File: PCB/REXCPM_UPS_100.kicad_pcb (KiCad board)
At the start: 2 copper layers, 51.3 x 18.3 mm, 7 parts, among them J1 Model_100_System_BUS, J2 Conn_01x03_Pin, U1 742G02

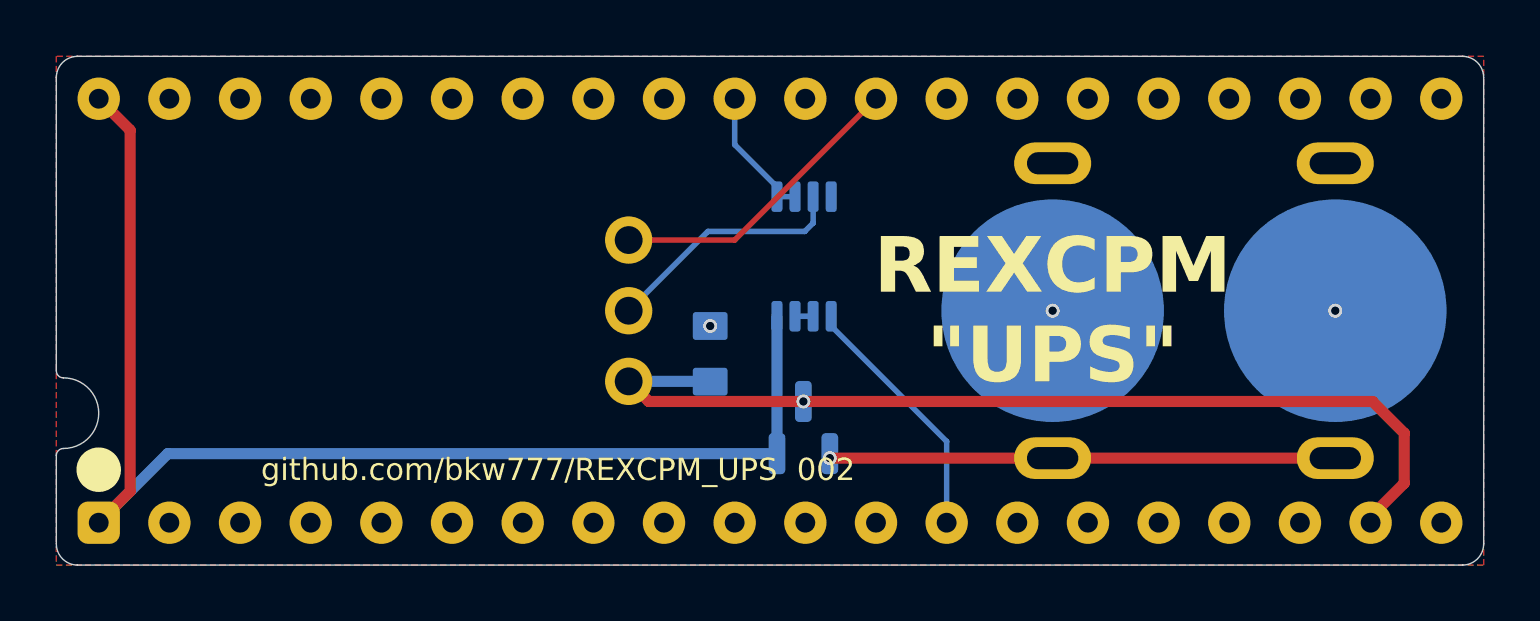
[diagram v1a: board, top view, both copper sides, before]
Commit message: m100 4 cells & jst-sh 4 pin
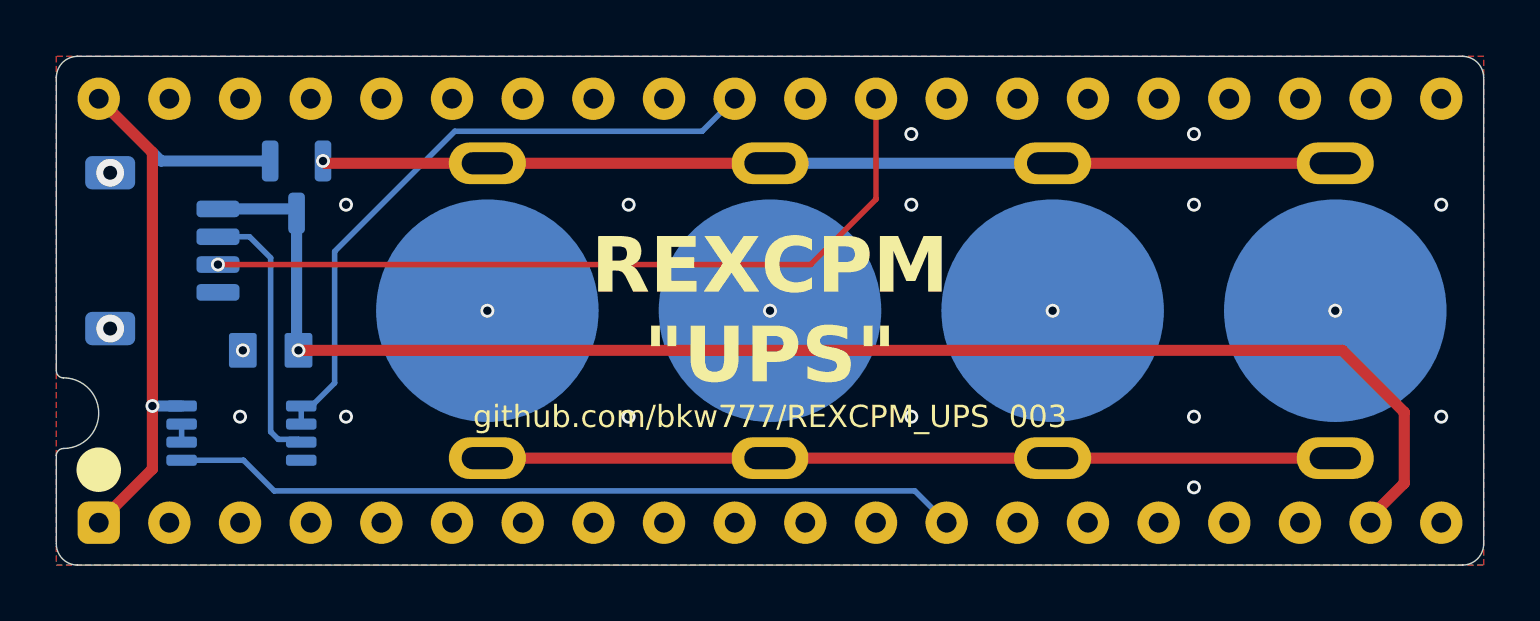
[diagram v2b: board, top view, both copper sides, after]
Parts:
- added BT3: Keystone_3031, 000_LOCAL:Keystone_3031, B.Cu at (136.5, 104.8)
- added BT4: Keystone_3031, 000_LOCAL:Keystone_3031, B.Cu at (126.4, 104.8)
- BT1: value BAT_3031 -> Keystone_3031
- J2: value Conn_01x03_Pin -> Conn_01x04_Pin; footprint 000_LOCAL:PinHeader_1x03_P2.54mm_Horizontal -> 000_LOCAL:JST_SH_SM04B-SRSS-TB_1x04-1MP_P1.00mm_Horizontal
- moved U1 21.2 mm to (117.5, 109.2), turned to 180 degrees
- moved D1 20.2 mm to (119.5, 100.3), turned to -90 degrees
- moved J2 16.8 mm to (114.7, 102.6), turned to 90 degrees
- moved C1 15.8 mm to (118.6, 106.2), turned to 180 degrees
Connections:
- D1 pad 1: /BATT+ -> VBUS
- D1 pad 2: VBUS -> /BATT+
- J2 pad 1: /~{WR} -> GND
- J2 pad 2: /RAM -> /~{WR}
- J2 pad 3: /RAM_RST -> /RAM
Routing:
- net /BATT+: track 18.2 -> 66.9 mm
- net VBUS: track 46.5 -> 25.0 mm, vias 0 -> 1
- net /IO/~{M}: track 9.14 -> 28.4 mm
- net /A15: track 4.80 -> 23.6 mm
- net /RAM_RST: track 35.3 -> 53.0 mm
- net /~{WR}: track 11.0 -> 28.2 mm, vias 0 -> 1
- net /RAM: track 8.88 -> 9.71 mm
- net GND: vias 3 -> 21
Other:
- board text removed: "RAM"
- board text removed: "RAM_RST"
- board text removed: "~{WR}"
